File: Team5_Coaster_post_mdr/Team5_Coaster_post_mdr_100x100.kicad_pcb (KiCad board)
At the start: 2 copper layers, 98.1 x 120 mm, 31 parts, among them J1 Vin, J10 GND, J11 GND, J12 GND, J13 3v3, J14 GND, J15 GND, J2 HC-05, J3 10V, J4 Batt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

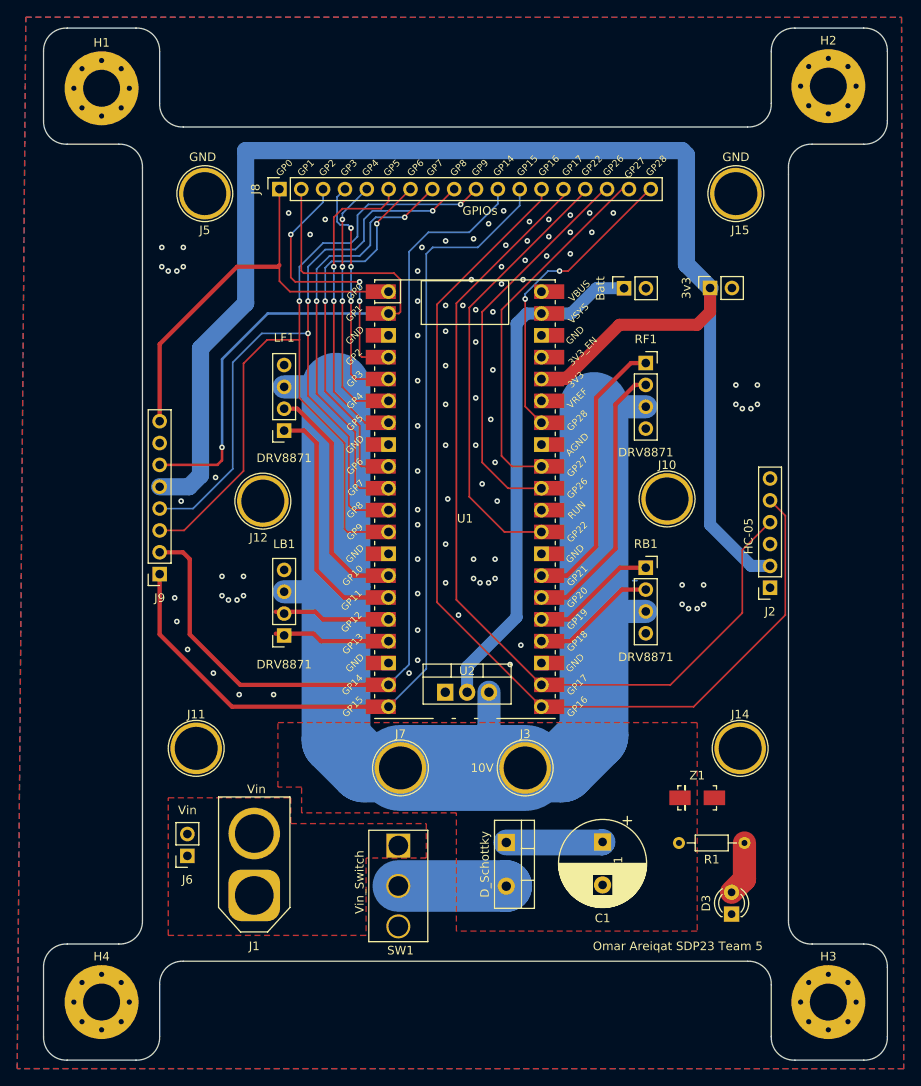
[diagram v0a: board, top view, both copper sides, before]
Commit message: Added 100x100 version of pcb
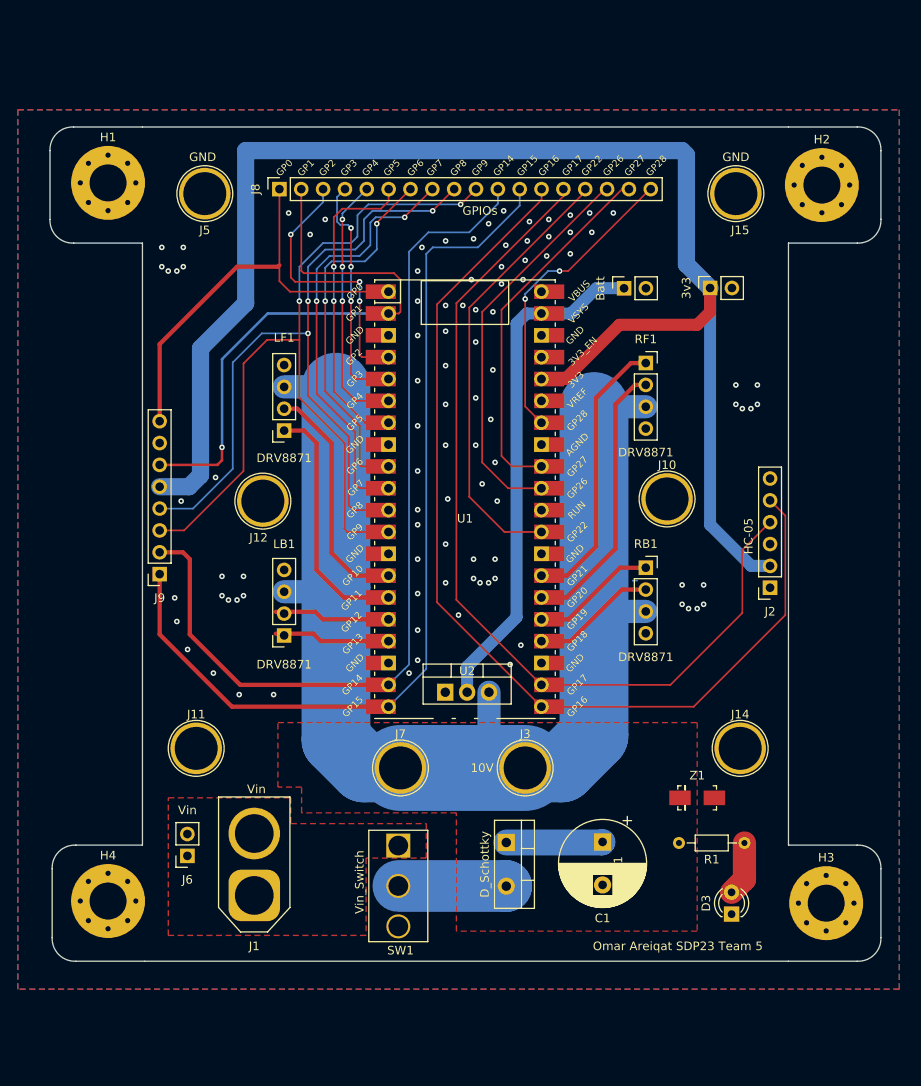
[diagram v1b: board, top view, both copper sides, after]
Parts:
- moved H4 11.8 mm to (85.2, 149.5)
- moved H2 11.5 mm to (168.2, 66.2)
- moved H3 11.5 mm to (168.8, 149.8)
- moved H1 11.0 mm to (85.2, 66.0)
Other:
- board size 98.1 x 120 mm -> 96.6 x 97 mm

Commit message: Added power zone
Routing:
- net +10V: track 158.3 -> 147.1 mm
- added copper zone on B.Cu, net Net-(D1-Pad2)
- added copper zone on F.Cu, net Net-(D1-Pad2)
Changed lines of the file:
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@@
   (segment (start 111.21 113.54) (end 111.75 113) (width 2.7) (layer "B.Cu") (net 3))
   (segment (start 147.775 115.83) (end 141.83 115.83) (width 2.7) (layer "B.Cu") (net 3))
-  (segment (start 142.686969 142.695354) (end 142.75 142.632323) (width 3) (layer "B.Cu") (net 3))
   (segment (start 105.725 89.72) (end 111.72 89.72) (width 2.7) (layer "B.Cu") (net 3))
-  (segment (start 131.555 142.695354) (end 142.686969 142.695354) (width 3) (layer "B.Cu") (net 3))
   (segment (start 141.75 130.27014) (end 141.75 115.75) (width 8) (layer "B.Cu") (net 3))
   (segment (start 115.00736 134.0275) (end 111.75 130.77014) (width 8) (layer "B.Cu") (net 3))
@@
     (polygon
       (pts
-        (xy 153.75 153)
-        (xy 125.75 153)
+        (xy 153.75 144)
+        (xy 125.75 144)
         (xy 125.75 139.25)
         (xy 107.75 139.25)
@@
       )
     )
+  )
+  (zone (net 11) (net_name "Net-(D1-Pad2)") (layers F&B.Cu) (hatch edge 0.508)
+    (connect_pads (clearance 0.508))
+    (min_thickness 0.254) (filled_areas_thickness no)
+    (fill yes (thermal_gap 0.508) (thermal_bridge_width 0.508))
+    (polygon
+      (pts
+        (xy 135.25 150.75)
+        (xy 115.75 150.75)
+        (xy 115.75 144.75)
+        (xy 135.25 144.75)
+      )
+    )

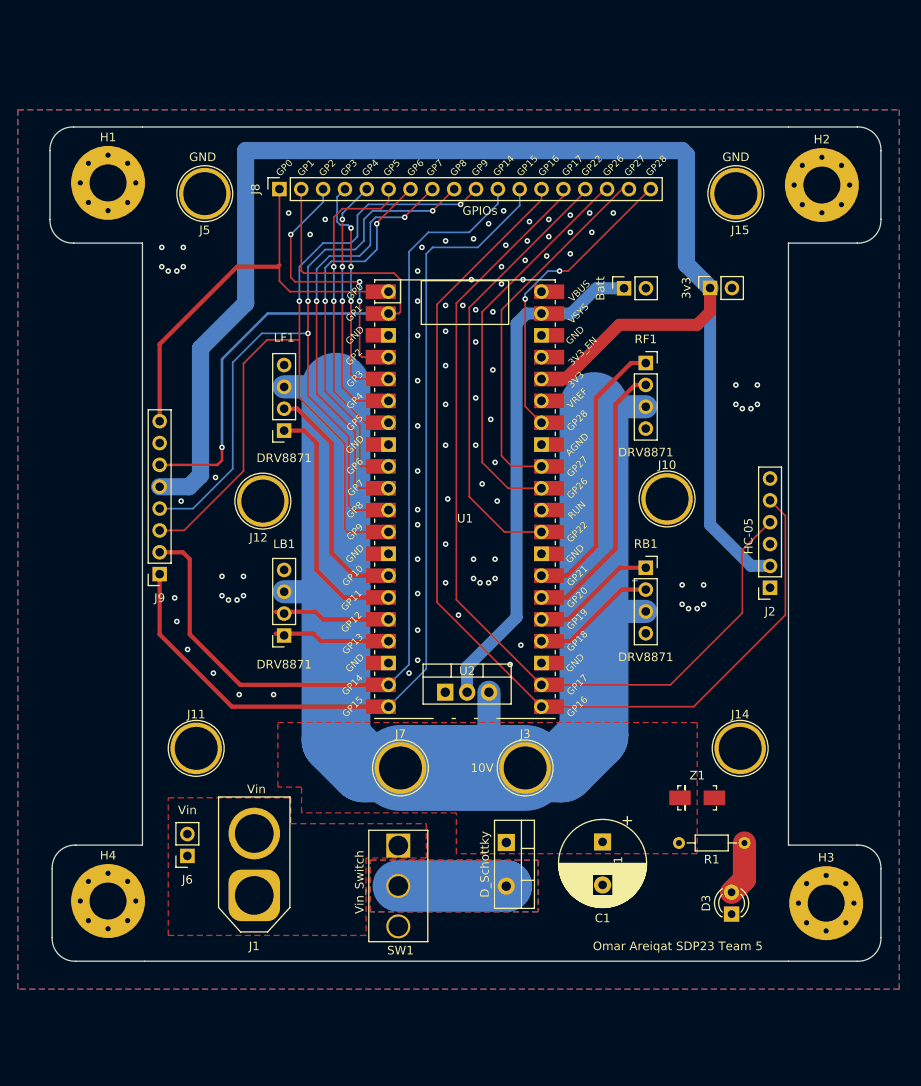
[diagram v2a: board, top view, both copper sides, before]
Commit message: Further updated power traces/zones on 100x100 pcb
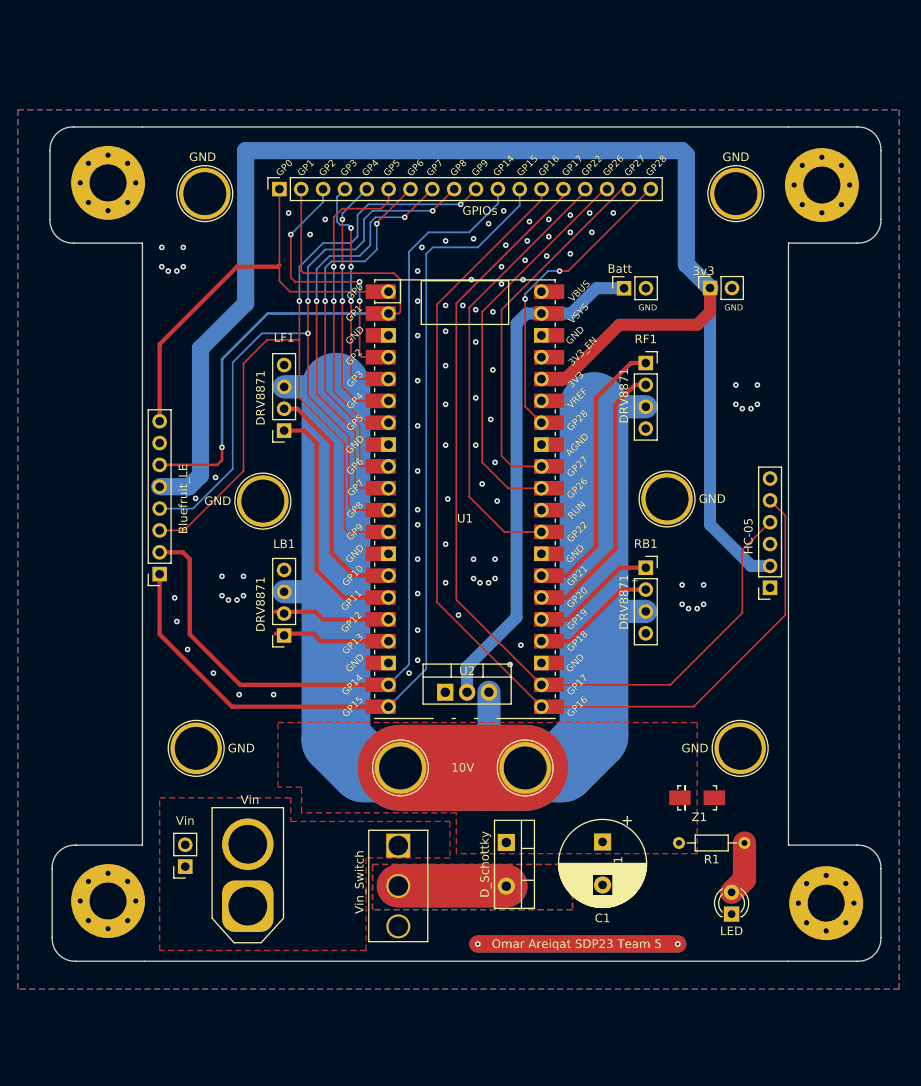
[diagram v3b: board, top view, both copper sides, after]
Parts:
- moved J1 1.46 mm to (101.5, 150.1)
- moved J6 1.27 mm to (94.2, 145.5)
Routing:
- net (no net): track 0.00 -> 46.5 mm, vias 0 -> 2
- net +10V: track 147.1 -> 161.6 mm
- net Net-(D1-Pad2): track 12.6 -> 25.1 mm
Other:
- board text added: "GND"

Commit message: did board auto cleanup
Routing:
- net GPIO2: track 32.0 -> 30.4 mm
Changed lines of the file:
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@@
       (drillshape 0)
       (scaleselection 1)
-      (outputdirectory "output/")
+      (outputdirectory "Coaster_Gerber/")
     )
   )
@@
   (segment (start 114.5 86) (end 114.5 79.75) (width 0.2) (layer "F.Cu") (net 27))
   (segment (start 116.2825 86.25) (end 114.75 86.25) (width 0.2) (layer "F.Cu") (net 27))
-  (segment (start 117.86 86.2675) (end 116.3 86.2675) (width 0.2) (layer "F.Cu") (net 27))
   (segment (start 114.75 86.25) (end 114.5 86) (width 0.2) (layer "F.Cu") (net 27))
-  (segment (start 116.3 86.2675) (end 116.2825 86.25) (width 0.2) (layer "F.Cu") (net 27))
   (segment (start 106.5 77) (end 106.5 72) (width 0.2) (layer "F.Cu") (net 27))
   (segment (start 114.5 77.5) (end 107 77.5) (width 0.2) (layer "F.Cu") (net 27))
@@
   (segment (start 114.5 101.5) (end 114 101) (width 0.2) (layer "F.Cu") (net 32))
   (segment (start 114 101) (end 114 95) (width 0.2) (layer "F.Cu") (net 32))
-  (segment (start 117.86 101.5075) (end 117.8525 101.5) (width 0.2) (layer "F.Cu") (net 32))
   (segment (start 119.75 70) (end 119.75 69.93) (width 0.2) (layer "F.Cu") (net 32))
   (segment (start 119.75 69.93) (end 122.955 66.725) (width 0.2) (layer "F.Cu") (net 32))
@@
   (segment (start 131.3375 106.5875) (end 127.25 102.5) (width 0.2) (layer "F.Cu") (net 36))
   (segment (start 135.64 106.5875) (end 131.3375 106.5875) (width 0.2) (layer "F.Cu") (net 36))
-  (segment (start 140.735 67.015) (end 140.735 66.725) (width 0.2) (layer "F.Cu") (net 36))
   (segment (start 127.25 80.5) (end 140.735 67.015) (width 0.2) (layer "F.Cu") (net 36))
-  (segment (start 143.025 66.725) (end 143.275 66.725) (width 0.2) (layer "F.Cu") (net 37))
   (segment (start 131.7575 101.5075) (end 128.75 98.5) (width 0.2) (layer "F.Cu") (net 37))
   (segment (start 128.75 98.5) (end 128.75 81) (width 0.2) (layer "F.Cu") (net 37))
@@
   (segment (start 137.75 76.25) (end 138.75 76.25) (width 0.2) (layer "F.Cu") (net 39))
   (segment (start 133.75 91.9975) (end 133.75 79.5) (width 0.2) (layer "F.Cu") (net 39))
-  (segment (start 148.275 66.725) (end 148.355 66.725) (width 0.2) (layer "F.Cu") (net 39))
   (segment (start 138.75 76.25) (end 148.275 66.725) (width 0.2) (layer "F.Cu") (net 39))
   (via (at 137.75 76.25) (size 0.65) (drill 0.3) (layers "F.Cu" "B.Cu") (net 39))
